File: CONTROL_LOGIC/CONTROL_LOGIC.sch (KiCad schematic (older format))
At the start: 42 parts, among them J1 Conn_01x02, J2 Conn_01x15, J3 Conn_01x24, J4 Conn_01x08, SW1 SW_Push, U1 74LS04, U2 74LS04, U3 74LS04

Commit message: Storage Registers added
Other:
- moved on the sheet: C1, C2, C3, C5, EEPROM1, EEPROM2, EEPROM3, J1, SW1, U3G

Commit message: Added Register
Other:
- moved on the sheet: C1, C2, C3, C5, EEPROM1, EEPROM2, EEPROM3, J1, SW1, U3G

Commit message: Updated Control Unit
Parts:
- removed D10, D11, D12, D13, D14, D15, D16, D17, D18, D19, D20, D21, D22, D23, D24, D3, D4, D5, D6, D7, D8, D9: LED, LED_THT:LED_D3.0mm, symbol Device:LED
- removed J3: Conn_01x24, Connector_PinHeader_2.54mm:PinHeader_1x24_P2.54mm_Vertical, symbol Connector_Generic:Conn_01x24
- removed RN1, RN2, RN3: R_Network08_US, Resistor_THT:R_Array_SIP9, symbol Device:R_Network08_US
- removed U2, U3: 74LS04, Package_DIP:DIP-14_W7.62mm, symbol 74xx:74LS04
- added BAR1, BAR2, BAR3: HDSP-4850_2, Display:HDSP-4850, symbol LED:HDSP-4830_2
- added C4: CP_Small, Capacitor_THT:C_Radial_D5.0mm_H7.0mm_P2.00mm, symbol Device:CP_Small
- added EEPROM4: AT28C256, Package_DIP:DIP-28_W15.24mm, symbol AT28C256:AT28C256
- added J10, J11: Conn_1x05, Connector_PinHeader_2.54mm:PinHeader_1x05_P2.54mm_Vertical, symbol Connector_Generic:Conn_01x05
- added J3, J7, J8: Conn_01x10, Connector_PinHeader_2.54mm:PinHeader_1x10_P2.54mm_Vertical, symbol Connector_Generic:Conn_01x10
- added J5: Screw_Terminal_01x02, TerminalBlock:TerminalBlock_bornier-2_P5.08mm, symbol Connector:Screw_Terminal_01x02
- added J6: Conn_01x15, Connector_PinHeader_2.54mm:PinHeader_1x15_P2.54mm_Vertical, symbol Connector_Generic:Conn_01x15
- added J9: Conn_01x02, Connector_PinHeader_2.54mm:PinHeader_1x02_P2.54mm_Vertical, symbol Connector_Generic:Conn_01x02
- added R1, R10, R11, R12, R13, R14, R15, R16, R17, R18, R19, R2, R20, R21, R22, R23, R24, R25, R26, R27, R28, R29, R3, R30, R31, R32, R4, R5, R6, R7, R8, R9: R_Small_US, Resistor_THT:R_Axial_DIN0204_L3.6mm_D1.6mm_P7.62mm_Horizontal, symbol Device:R_Small_US
- J4: value Conn_01x08 -> Conn_2x08; footprint Connector_PinHeader_2.54mm:PinHeader_1x08_P2.54mm_Vertical -> Connector_PinHeader_2.54mm:PinHeader_2x08_P2.54mm_Vertical; symbol Connector_Generic:Conn_01x08 -> Connector_Generic:Conn_02x08_Top_Bottom
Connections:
- net labels added: D25, D26, D27, D28, D29, D30, D31, D32
- wire segments 188 -> 297
- no-connect marks 8 -> 0
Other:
- moved on the sheet: C5, SW1

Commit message: Adding Control Logic Module
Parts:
- EEPROM1, EEPROM2, EEPROM3, EEPROM4: symbol AT28C256:AT28C256 -> CONTROL_LOGIC-rescue:AT28C256-AT28C256
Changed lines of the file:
@@
 Connection ~ 2250 1700
 $Comp
-L AT28C256:AT28C256 EEPROM1
+L CONTROL_LOGIC-rescue:AT28C256-AT28C256 EEPROM1
 U 1 1 609F1420
 P 3550 3400
@@
 	4150 2800 4150 2550
 $Comp
-L AT28C256:AT28C256 EEPROM2
+L CONTROL_LOGIC-rescue:AT28C256-AT28C256 EEPROM2
 U 1 1 60B559F9
 P 5250 3400
@@
 	5850 2800 5850 2550
 $Comp
-L AT28C256:AT28C256 EEPROM3
+L CONTROL_LOGIC-rescue:AT28C256-AT28C256 EEPROM3
 U 1 1 60B6AB22
 P 6950 3400
@@
 	8850 4200 8850 4000
 $Comp
-L AT28C256:AT28C256 EEPROM4
+L CONTROL_LOGIC-rescue:AT28C256-AT28C256 EEPROM4
 U 1 1 609ED830
 P 8650 3400

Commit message: Updated to Control Logic board
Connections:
- wire segments 297 -> 299
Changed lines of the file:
@@
 L Connector_Generic:Conn_01x05 J?
 U 1 1 61226356
-P 11100 2950
+P 11050 2950
 AR Path="/609D754A/61226356" Ref="J?"  Part="1"
 AR Path="/61226356" Ref="J11"  Part="1"
-F 0 "J11" V 10972 3330 50  0001 L CNN
-F 1 "Conn_1x05" V 11063 3330 50  0001 L CNN
-F 2 "Connector_PinHeader_2.54mm:PinHeader_1x05_P2.54mm_Vertical" H 11100 2950 50  0001 C CNN
-F 3 "~" H 11100 2950 50  0001 C CNN
-	1    11100 2950
-	1    0    0    -1
+F 0 "J11" V 10922 3330 50  0001 L CNN
+F 1 "Conn_1x05" V 11013 3330 50  0001 L CNN
+F 2 "Connector_PinHeader_2.54mm:PinHeader_1x05_P2.54mm_Vertical" H 11050 2950 50  0001 C CNN
+F 3 "~" H 11050 2950 50  0001 C CNN
+	1    11050 2950
+	-1   0    0    1
 $EndComp
 Wire Wire Line
@@
 	10850 2650 10850 2850
 Wire Wire Line
-	10850 2850 10900 2850
-Wire Wire Line
 	10700 3050 10750 3050
 Wire Wire Line
 	10750 3050 10750 2950
-Wire Wire Line
-	10750 2950 10900 2950
-Wire Wire Line
-	10900 3050 10800 3050
 Wire Wire Line
 	10800 3050 10800 3500
@@
 Wire Wire Line
 	5400 5800 5450 5800
+Wire Wire Line
+	10900 2750 11250 2750
+Wire Wire Line
+	10850 2850 11250 2850
+Wire Wire Line
+	10750 2950 11250 2950
+Wire Wire Line
+	10800 3050 11250 3050
+Wire Wire Line
+	11250 3150 10900 3150
 $EndSCHEMATC

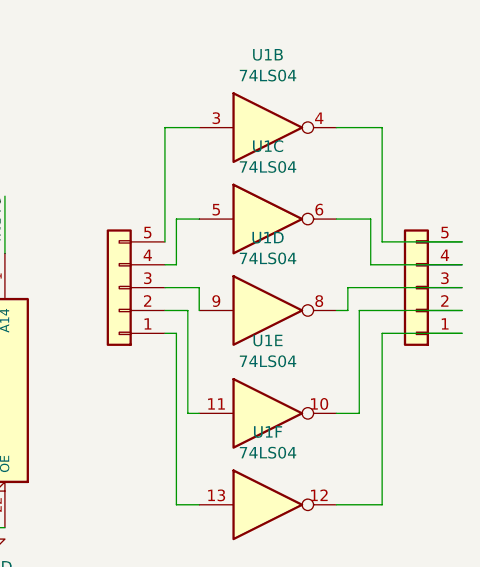
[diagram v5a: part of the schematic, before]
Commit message: Updating RAM Programmer
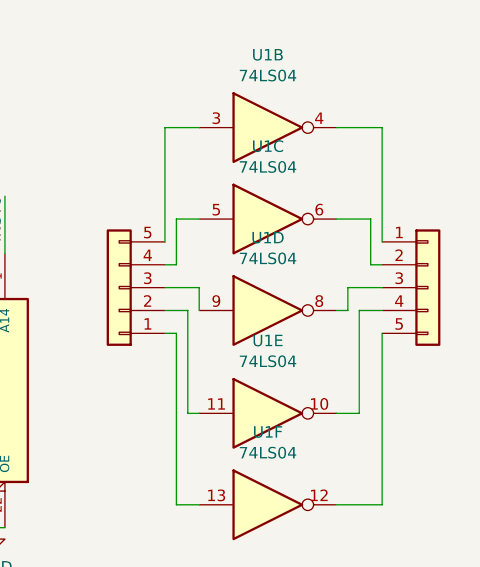
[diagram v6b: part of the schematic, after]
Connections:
- wire segments 299 -> 297
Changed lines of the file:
@@
 Wire Wire Line
 	10000 3900 10100 3900
-$Comp
-L Connector_Generic:Conn_01x05 J?
-U 1 1 61226356
-P 11050 2950
-AR Path="/609D754A/61226356" Ref="J?"  Part="1"
-AR Path="/61226356" Ref="J11"  Part="1"
-F 0 "J11" V 10922 3330 50  0001 L CNN
-F 1 "Conn_1x05" V 11013 3330 50  0001 L CNN
-F 2 "Connector_PinHeader_2.54mm:PinHeader_1x05_P2.54mm_Vertical" H 11050 2950 50  0001 C CNN
-F 3 "~" H 11050 2950 50  0001 C CNN
-	1    11050 2950
-	-1   0    0    1
-$EndComp
 Wire Wire Line
 	10900 2750 10900 2250
@@
 	5400 5800 5450 5800
 Wire Wire Line
-	10900 2750 11250 2750
-Wire Wire Line
-	10850 2850 11250 2850
-Wire Wire Line
-	10750 2950 11250 2950
-Wire Wire Line
-	10800 3050 11250 3050
-Wire Wire Line
-	11250 3150 10900 3150
+	10900 3050 10800 3050
+Wire Wire Line
+	10750 2950 10900 2950
+Wire Wire Line
+	10850 2850 10900 2850
+$Comp
+L Connector_Generic:Conn_01x05 J?
+U 1 1 61226356
+P 11100 2950
+AR Path="/609D754A/61226356" Ref="J?"  Part="1"
+AR Path="/61226356" Ref="J11"  Part="1"
+F 0 "J11" V 10972 3330 50  0001 L CNN
+F 1 "Conn_1x05" V 11063 3330 50  0001 L CNN
+F 2 "Connector_PinHeader_2.54mm:PinHeader_1x05_P2.54mm_Vertical" H 11100 2950 50  0001 C CNN
+F 3 "~" H 11100 2950 50  0001 C CNN
+	1    11100 2950
+	1    0    0    -1
+$EndComp
 $EndSCHEMATC

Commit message: Updating components
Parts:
- removed C1, C3, C4: CP_Small, Capacitor_THT:C_Radial_D5.0mm_H7.0mm_P2.00mm, symbol Device:CP_Small
- removed J7, J8: Conn_01x10, Connector_PinHeader_2.54mm:PinHeader_1x10_P2.54mm_Vertical, symbol Connector_Generic:Conn_01x10
- removed R1, R10, R11, R12, R13, R14, R15, R16, R17, R18, R19, R2, R20, R21, R22, R23, R24, R25, R26, R27, R28, R29, R3, R30, R31, R32, R4, R5, R6, R7, R8, R9: R_Small_US, Resistor_THT:R_Axial_DIN0204_L3.6mm_D1.6mm_P7.62mm_Horizontal, symbol Device:R_Small_US
- added J7: Conn_1x08, Connector_PinHeader_2.54mm:PinHeader_1x08_P2.54mm_Vertical, symbol Connector_Generic:Conn_01x08
- added J8: Conn_01x10, Connector_PinHeader_2.54mm:PinHeader_1x30_P2.54mm_Vertical, symbol Connector_Generic:Conn_01x30
- added RN14, RN15, RN16, RN17: R_Network08_US, Resistor_THT:R_Array_SIP9, symbol Device:R_Network08_US
- EEPROM1, EEPROM2, EEPROM3, EEPROM4: footprint Package_DIP:DIP-28_W15.24mm -> Socket:DIP_Socket-40_W11.9_W12.7_W15.24_W17.78_W18.5_3M_240-1280-00-0602J
- J3: footprint Connector_PinHeader_2.54mm:PinHeader_1x10_P2.54mm_Vertical -> Connector_PinHeader_2.54mm:PinHeader_1x30_P2.54mm_Vertical; symbol Connector_Generic:Conn_01x10 -> Connector_Generic:Conn_01x30
- J50: renamed from J5; footprint TerminalBlock:TerminalBlock_bornier-2_P5.08mm -> TerminalBlock_Phoenix:TerminalBlock_Phoenix_MKDS-1,5-2_1x02_P5.00mm_Horizontal
- renumbered D1 to D79, D2 to D80, SW1 to SW6, U1 to U7
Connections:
- net labels added: μ1, μ10, μ11, μ12, μ13, μ14, μ15, μ16, μ17, μ18, μ19, μ2, μ20, μ21, μ22, μ23, μ24, μ25, μ26, μ27, μ28, μ29, μ3, μ30, μ31, μ32, μ4, μ5, μ6, μ7, μ8, μ9
- wire segments 297 -> 237
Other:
- note added: "CONNECTIONS"
- note added: "EEPROMS"
- note added: "LED Display"
- note added: "POWER"
- note added: "RESET & INVERT"
- note added: "SPARE INVERTER PINS"
- note removed: "RESET"
- moved on the sheet: C25, C26, EEPROM1, EEPROM2, EEPROM3, EEPROM4, J49, J50, SW6, U7B, U7C, U7D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
